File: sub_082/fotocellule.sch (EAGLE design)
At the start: 24 parts, among them IC1 TL082P, IC3 LM555N, T1 BD647

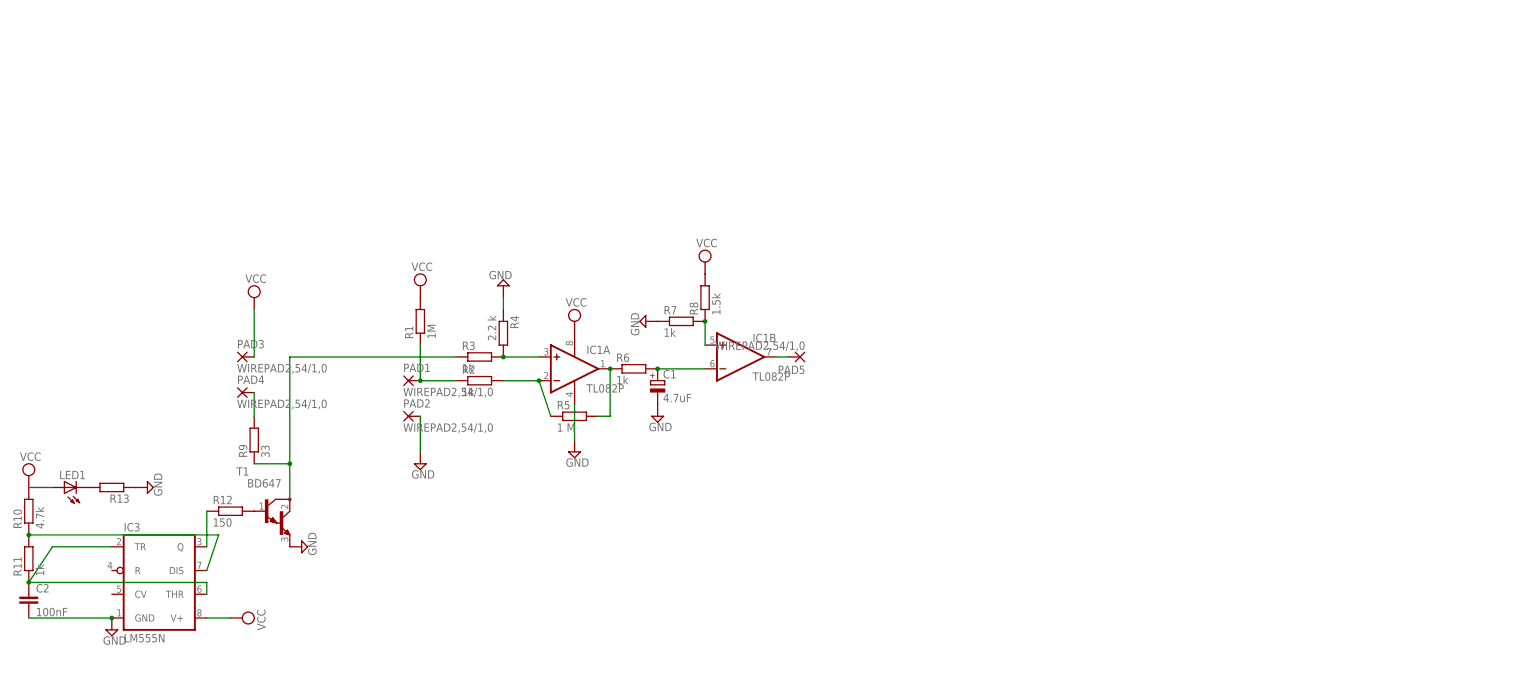
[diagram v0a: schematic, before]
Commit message: Risistemati i due progetti per l'utilizzo dei singoli/doppi opamp
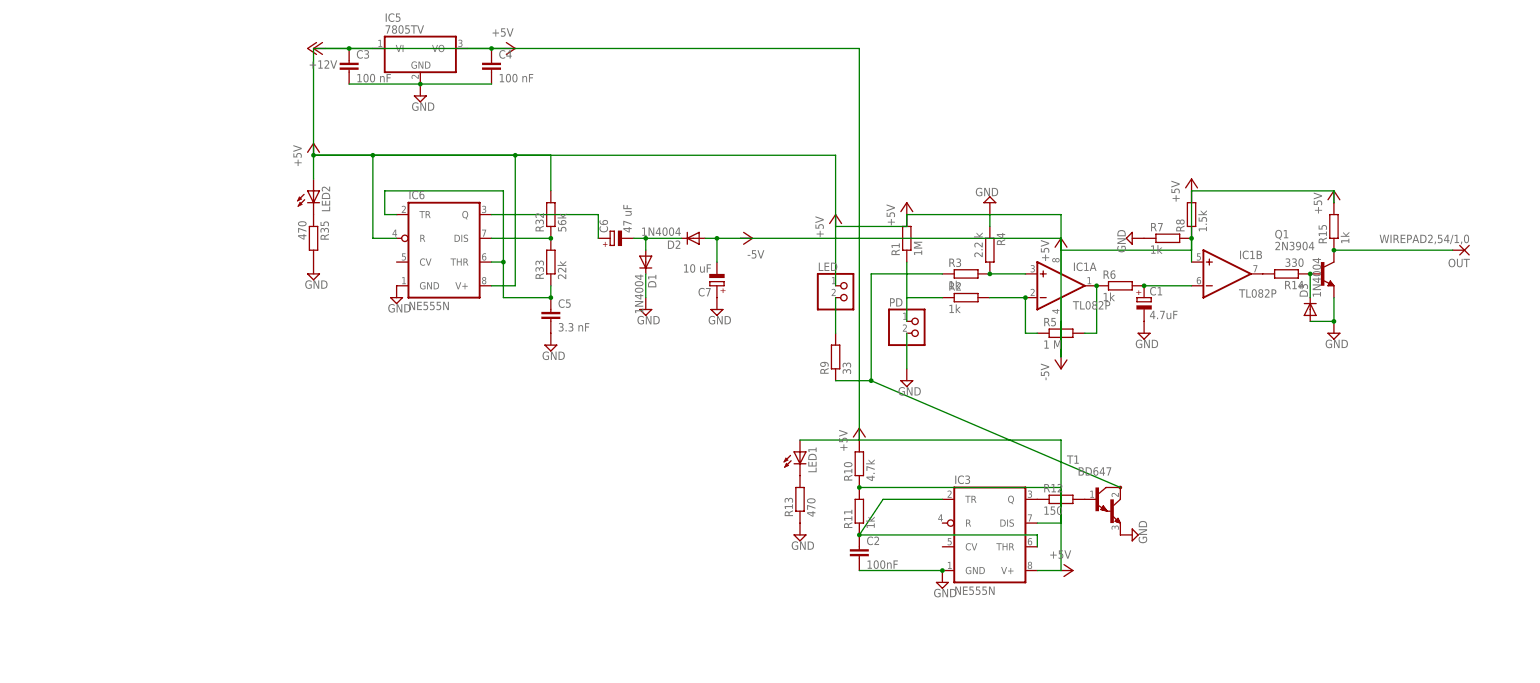
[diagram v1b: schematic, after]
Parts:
- removed PAD1, PAD2, PAD3, PAD4, PAD5: WIREPAD2,54/1,0, wirepad:WIREPAD2,54/1,0
- added C3, C4: 100 nF, resistor:C-EU025-024X044
- added C5: 3.3 nF, resistor:C-EU025-024X044
- added C6: 47 uF, rcl:CPOL-EUE2.5-5
- added C7: 10 uF, rcl:CPOL-EUE2.5-5
- added D1, D2, D3: 1N4004, diode:1N4004
- added IC5: 7805TV, linear:7805TV
- added IC6: NE555N, linear:NE555N
- added LED, PD: (no value), pinhead:PINHD-1X2
- added LED2: (no value), led:LED5MM
- added OUT: WIREPAD2,54/1,0, wirepad:WIREPAD2,54/1,0
- added Q1: 2N3904, transistor-npn:2N3904
- added R14: 330, resistor:R-EU_0207/10
- added R15: 1k, resistor:R-EU_0207/10
- added R32: 56k, resistor:R-EU_0207/10
- added R33: 22k, resistor:R-EU_0207/10
- added R35: 470, resistor:R-EU_0207/10
- IC3: value LM555N -> NE555N; device linear:LM555N -> linear:NE555N
- R13: value (none) -> 470
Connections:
- new net +5V: C4.1, IC1P.V+, IC3.V+, IC5.VO, IC6.R, IC6.V+, LED.1, LED1.A, LED2.A, R1.2, R10.2, R15.2, R32.2, R8.2
- new net -5V: C7.-, D2.A, IC1P.V-
- new net N$16: OUT.P, Q1.C, R15.1
- new net N$18: D3.C, Q1.B, R14.1
- new net N$32: LED2.C, R35.1
- new net N$33: C6.+, IC6.Q
- new net N$34: C5.1, IC6.THR, IC6.TR, R33.1
- new net N$35: C6.-, D1.A, D2.C
- new net N$8: IC6.DIS, R32.1, R33.2
- net GND: now also C3.2, C4.2, C5.2, C7.+, D1.C, D3.A, IC5.GND, IC6.GND, PD.2, Q1.E, R35.2; no longer IC1P.V-, PAD2.P
- net N$1: now also PD.1; no longer PAD1.P
- net N$13: now also R14.2; no longer PAD5.P
- net N$7: now also LED.2; no longer PAD4.P
- net VCC: now also C3.1, IC5.VI; no longer IC1P.V+, IC3.V+, LED1.A, PAD3.P, R1.2, R10.2, R8.2
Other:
- moved on the sheet: C1, C2, IC1A, IC1B, IC3, LED1, R1, R10, R11, R12, R13, R2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

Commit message: Rewired correctly sub082
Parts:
- removed IC5: 7805TV, linear:7805TV
- removed IC6: NE555N, linear:NE555N
- removed LED, PD: (no value), pinhead:PINHD-1X2
- removed OUT: WIREPAD2,54/1,0, wirepad:WIREPAD2,54/1,0
- removed R32: 56k, resistor:R-EU_0207/10
- removed R33: 22k, resistor:R-EU_0207/10
- removed R35: 470, resistor:R-EU_0207/10
- added IC2: NE555N, linear:NE555N
- added IC4: TL082P, linear:TL082P
- added JP1: POWER_JACKPTH_LOCK, SparkFun-Connectors:POWER_JACKPTH_LOCK
- added LEDP1, LEDP2, LEDP3, LEDP4, OUT1, PD1: (no value), pinhead:PINHD-1X2
- added Q2: IRF530, transistor-power:IRF530
- added R16: 1 M, resistor:R-EU_0207/10
- added R17, R18, R21: 1k, resistor:R-EU_0207/10
- added R19: 1.5k, resistor:R-EU_0207/10
- added R20: 330, resistor:R-EU_0207/10
- C1: value 4.7uF -> 100nF; device resistor:CPOL-EUE2.5-6 -> resistor:C-EU025-024X044
- C2: value 100nF -> 3.3 nF
- C3: value 100 nF -> 330 nF
- C5: value 3.3 nF -> 47 uF; device resistor:C-EU025-024X044 -> rcl:CPOL-EUE2.5-5
- C6: value 47 uF -> 10 uF
- C7: value 10 uF -> 4.7uF; device rcl:CPOL-EUE2.5-5 -> resistor:CPOL-EUE2.5-6
- IC1: value TL082P -> NE555N; device linear:TL082P -> linear:NE555N
- IC3: value NE555N -> 7805TV; device linear:NE555N -> linear:7805TV
- R1: value 1M -> 470
- R10: value 4.7k -> 33
- R11: value 1k -> 33
- R12: value 150 -> 1M
- R13: value 470 -> 1k
- R14: value 330 -> 1k
- R15: value 1k -> 2.2 k
- R2: value 1k -> 470
- R3: value 1k -> 4.7k
- R4: value 2.2 k -> 1k
- R5: value 1 M -> 56k
- R6: value 1k -> 22k
- R7: value 1k -> 150
- R8: value 1.5k -> 33
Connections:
- removed net N$33: C6.+, IC6.Q
- removed net N$34: C5.1, IC6.THR, IC6.TR, R33.1
- removed net N$35: C6.-, D1.A, D2.C
- removed net VCC: C3.1, IC5.VI
- new net LEDSIG: Q2.D, R10.1, R11.1, R13.1, R8.1, R9.1
- new net N$11: C5.-, D1.A, D2.C
- new net N$17: LEDP2.2, R9.2
- new net N$19: LEDP3.2, R10.2
- new net N$20: LEDP4.2, R11.2
- new net N$21: IC4A.-IN, R14.2, R16.1
- new net VIN: C3.1, IC3.VI, JP1.PWR
- net +5V: now also IC1.R, IC1.V+, IC2.R, IC2.V+, IC3.VO, IC4P.V+, LEDP1.1, LEDP2.1, LEDP3.1, LEDP4.1, R12.2, R19.2, R21.2, R3.2, R5.2; no longer IC1P.V+, IC3.V+, IC5.VO, IC6.R, IC6.V+, LED.1, R1.2, R10.2, R15.2, R32.2, R8.2
- net -5V: now also C6.-, IC4P.V-; no longer C7.-, IC1P.V-
- net GND: now also C1.2, C6.+, C7.-, IC1.GND, IC2.GND, JP1.GND, JP1.GNDBREAK, OUT1.2, PD1.2, Q2.S, R1.1, R15.1, R18.1, R2.2; no longer C1.-, C5.2, C7.+, IC5.GND, IC6.GND, PD.2, R13.1, R35.2, R4.1, R7.1, T1.E
- net N$1: now also C1.1, IC2.THR, IC2.TR, R4.1; no longer PD.1, R1.1, R2.1
- net N$10: now also C5.+, IC1.Q; no longer C2.1, IC3.THR, IC3.TR, R11.1
- net N$12: now also Q2.G, R7.2; no longer R12.2, T1.B
- net N$13: now also IC4B.OUT, R20.2; no longer IC1B.OUT, R14.2
- net N$14: now also R1.2; no longer R13.2
- net N$15: now also LEDP1.2, R8.2; no longer IC3.DIS, R10.1, R11.2
- net N$16: now also OUT1.1, R21.1; no longer OUT.P, R15.1
- net N$18: now also R20.1; no longer R14.1
- net N$2: now also IC2.DIS, R3.1, R4.2; no longer IC1A.-IN, R2.2, R5.1
- net N$22: now also PD1.1, R12.1, R14.1; no longer R3.1, R9.1, T1.C
- net N$3: now also IC4A.+IN, R13.2, R15.2; no longer IC1A.+IN, R3.2, R4.2
- net N$32: now also R2.1; no longer R35.1
- net N$4: now also IC4A.OUT, R16.2, R17.1; no longer IC1A.OUT, R5.2, R6.1
- net N$5: now also C7.+, IC4B.-IN, R17.2; no longer C1.+, IC1B.-IN, R6.2
- net N$6: now also IC4B.+IN, R18.2, R19.1; no longer IC1B.+IN, R7.2, R8.1
- net N$7: now also C2.1, IC1.THR, IC1.TR, R6.1; no longer LED.2, R9.2
- net N$8: now also IC1.DIS, R5.1, R6.2; no longer IC6.DIS, R32.1, R33.2
- net N$9: now also IC2.Q, R7.1; no longer IC3.Q, R12.1
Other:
- moved on the sheet: C2, C3, C4, C6, C7, D1, D2, D3, LED1, LED2, Q1, R1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
